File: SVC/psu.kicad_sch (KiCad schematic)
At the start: 32 parts, among them T1 760871543, U10 FODM217D, U11 TNY288D, U12 SI8932D-IS4, U13 AP7381-33SA-7

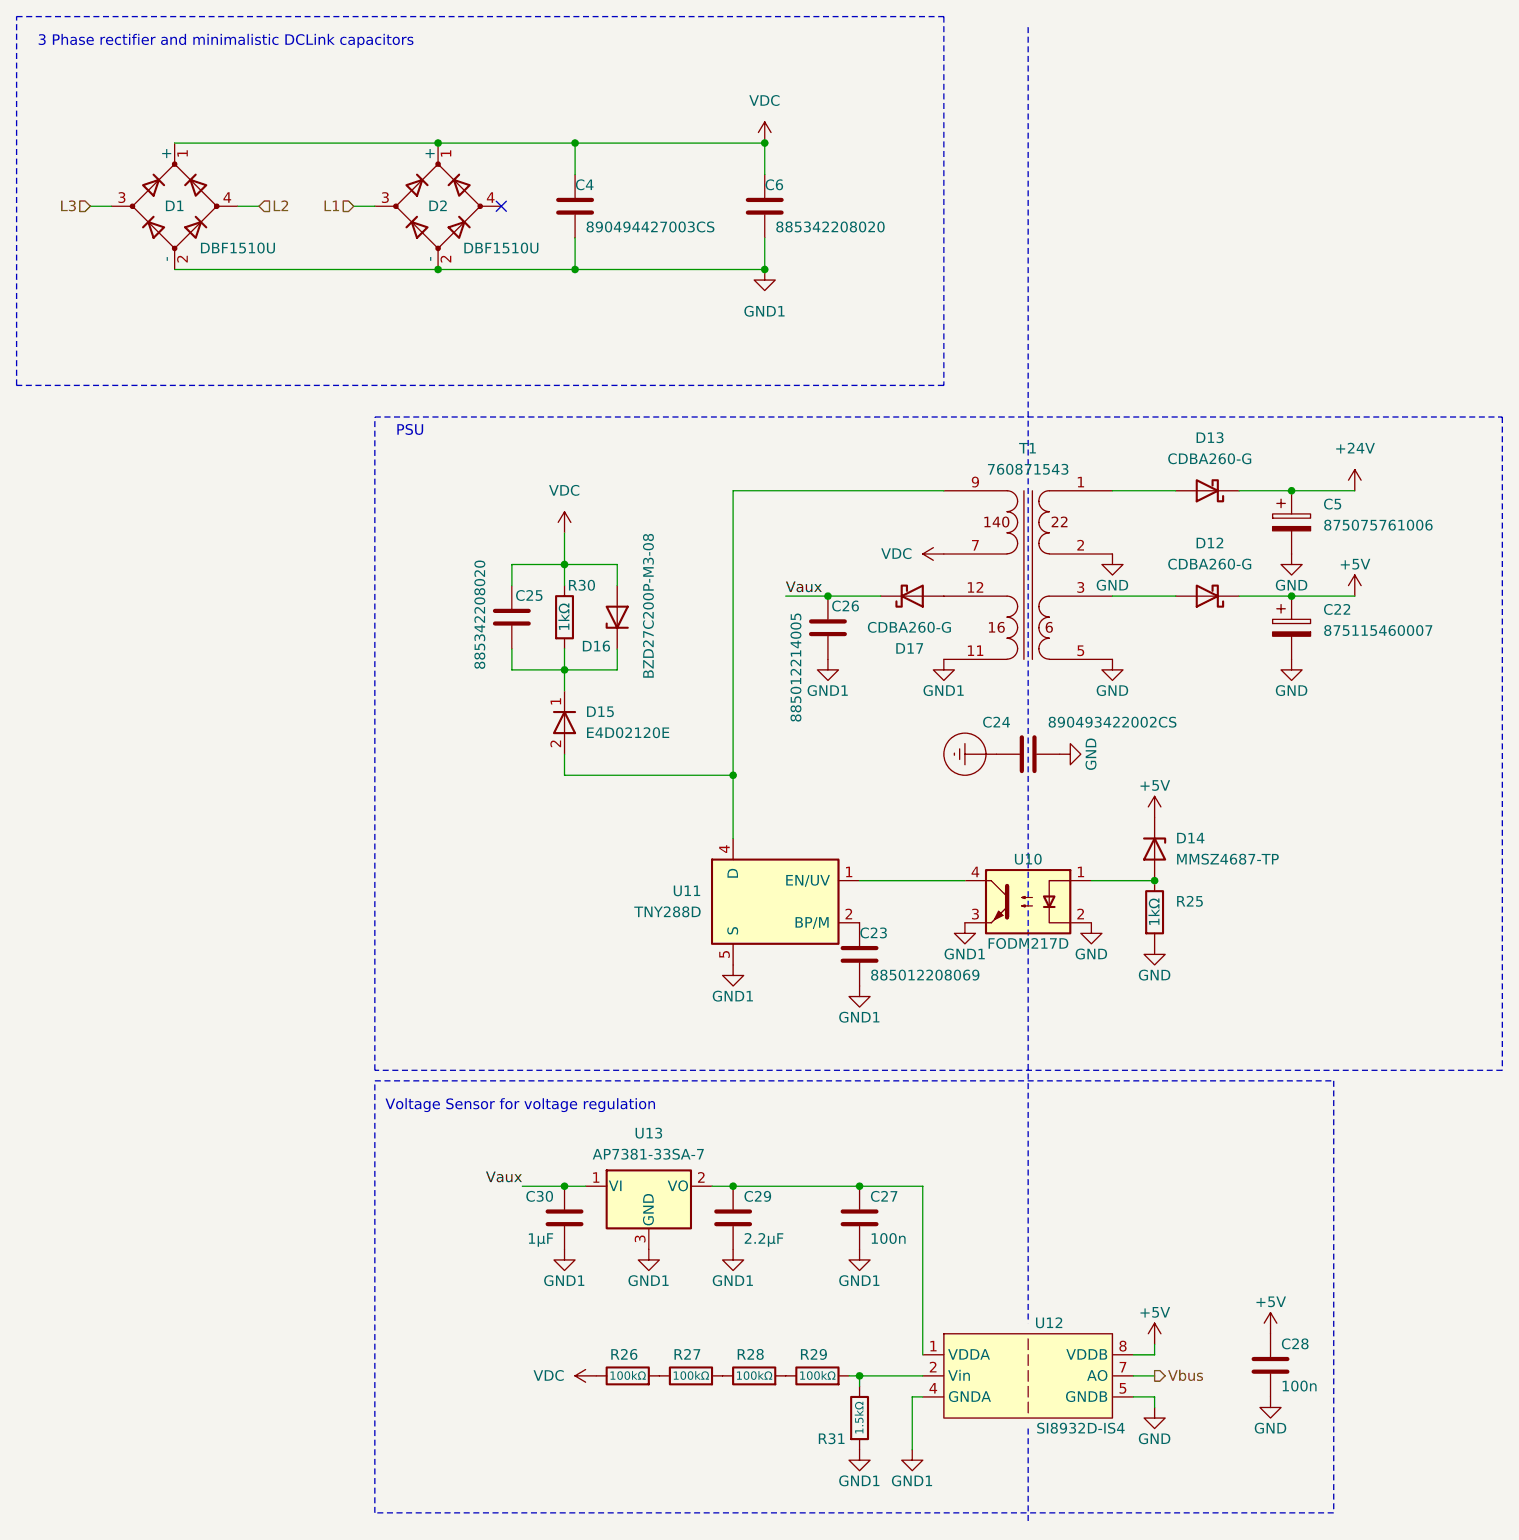
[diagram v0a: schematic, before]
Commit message: did some layout work, minor schematic changes to help with layout
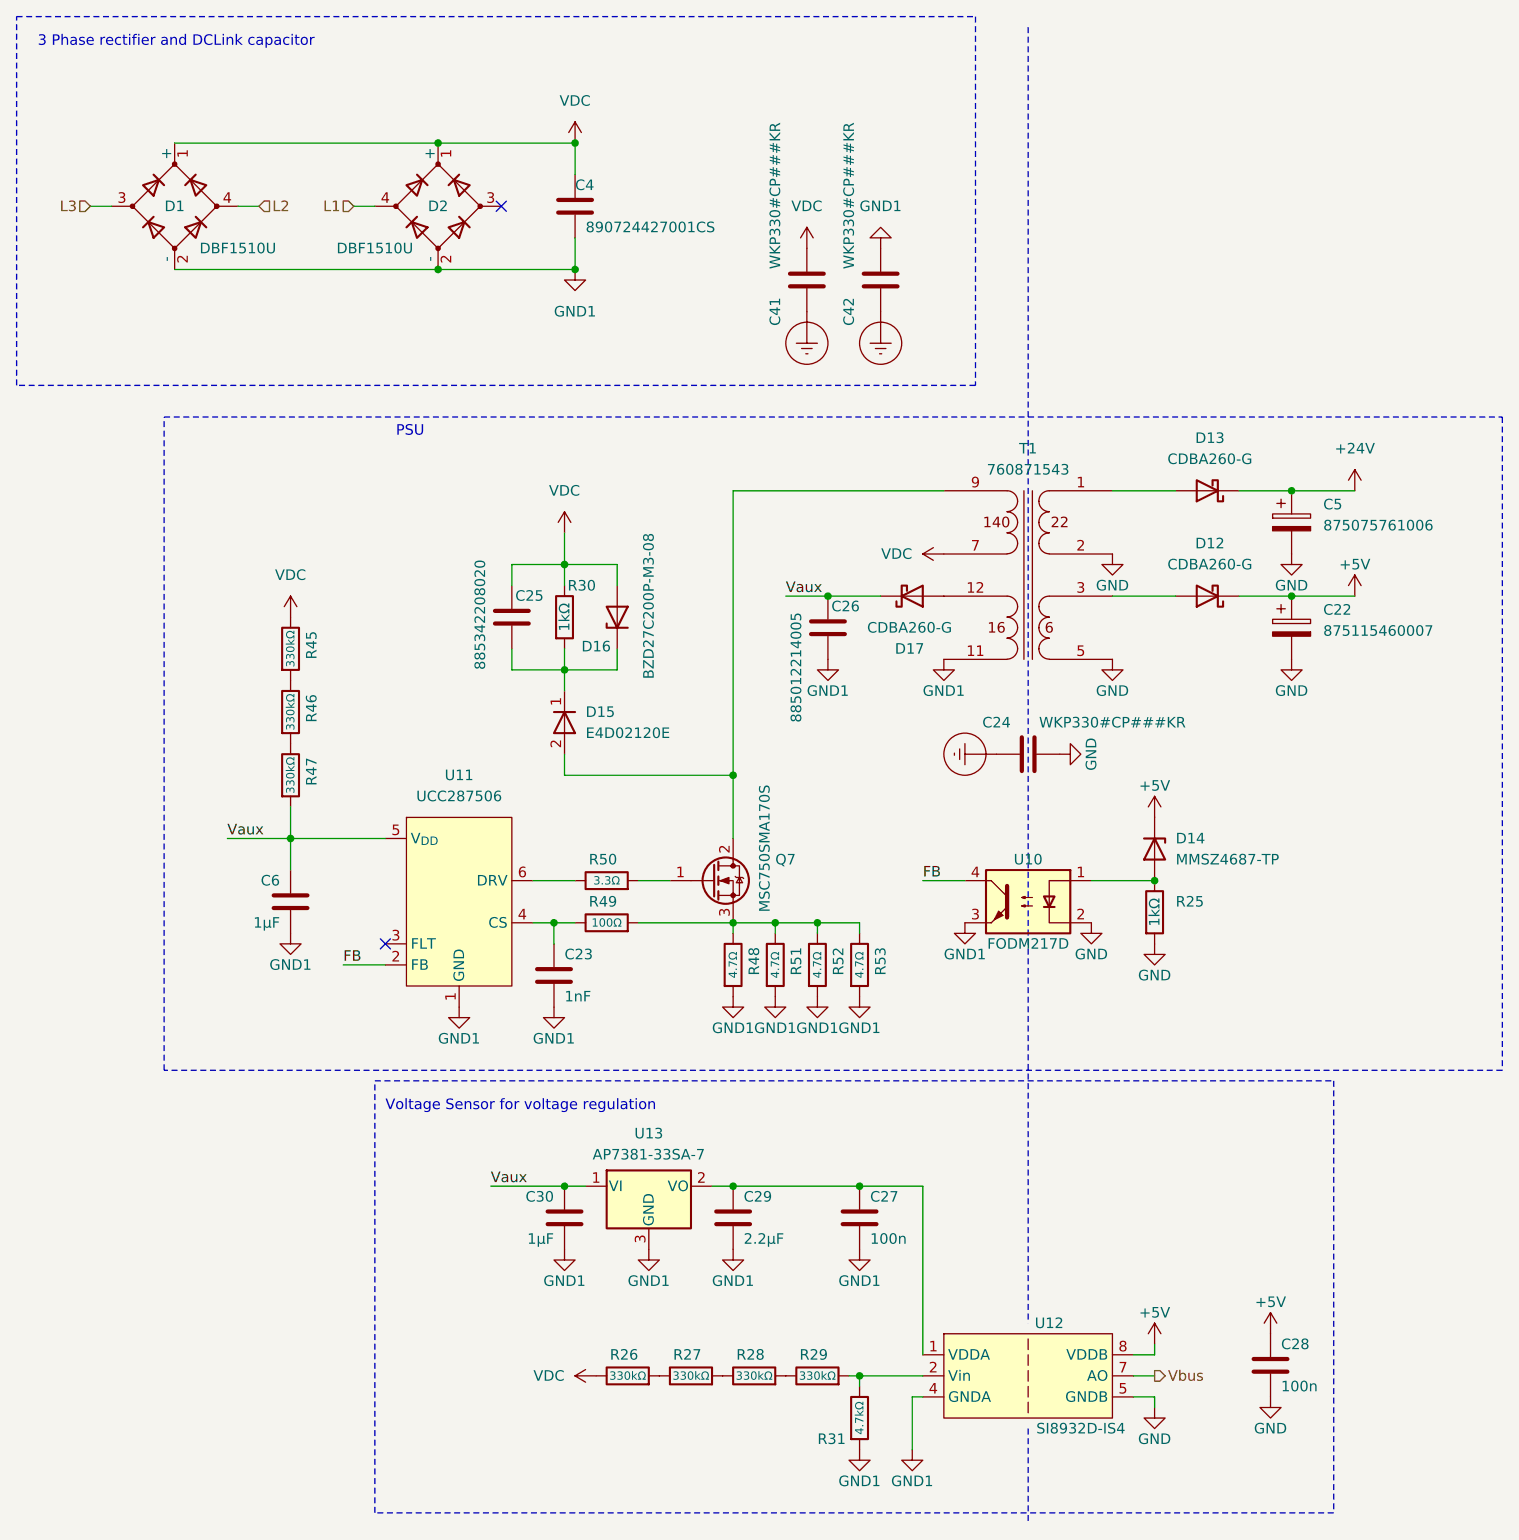
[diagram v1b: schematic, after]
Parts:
- removed U11: TNY288D, Package_SO:PowerIntegrations_SO-8C, symbol Regulator_Switching:TNY288D
- added C41, C42: WKP330#CP###KR, Footprints:WKP330#CP###KR, symbol Device:C
- added Q7: MSC750SMA170S, Package_TO_SOT_SMD:TO-252-2, symbol Device:Q_NMOS_GDS
- added R45, R46, R47: 330kΩ, Resistor_SMD:R_0805_2012Metric, symbol Device:R
- added R48, R51, R52, R53: 4.7Ω, Resistor_SMD:R_0805_2012Metric, symbol Device:R
- added R49: 100Ω, Resistor_SMD:R_0805_2012Metric, symbol Device:R
- added R50: 3.3Ω, Resistor_SMD:R_0805_2012Metric, symbol Device:R
- added U11: UCC287506, Package_TO_SOT_SMD:SOT-23-6, symbol parts:UCC28750X
- C23: value 885012208069 -> 1nF; footprint Capacitor_SMD:C_1206_3216Metric -> Capacitor_SMD:C_0805_2012Metric
- C24: value 890493422002CS -> WKP330#CP###KR; footprint Capacitor_THT:C_Rect_L10.3mm_W5.7mm_P7.50mm_MKS4 -> Footprints:WKP330#CP###KR
- C4: value 890494427003CS -> 890724427001CS; footprint Capacitor_THT:C_Rect_L33.0mm_W15.0mm_P27.50mm_MKS4 -> Capacitor_THT:C_Rect_L31.5mm_W9.0mm_P27.50mm_MKS4
- C6: value 885342208020 -> 1µF; footprint Capacitor_SMD:C_1206_3216Metric -> Capacitor_SMD:C_0805_2012Metric
- R26, R27, R28, R29: value 100kΩ -> 330kΩ
- R30: footprint Resistor_SMD:R_0805_2012Metric -> Resistor_SMD:R_1206_3216Metric
- R31: value 1.5kΩ -> 4.7kΩ
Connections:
- net Earth_Protective: now also C41.1, C42.1
- net GND1: now also C42.2, R48.2, R51.2, R52.2, R53.2, U11.1 (GND)
- net L1: now also D2.4; no longer D2.3
- net VDC: now also C41.2, R45.1; no longer C6.1
- net Vaux: now also C6.1, R47.2, U11.5 (V_{DD})
- net FB: now reaches U10.4
- net FB: now also U11.2 (FB)
- net at C23.1: now also R49.1, U11.4 (CS)
- net at D15.2 (A), T1.9 (IN+): now also Q7.2 (D)
- new net: Q7.3 (S), R48.1, R49.2, R51.1, R52.1, R53.1
- new net: R45.2, R46.1
- new net: R46.2, R47.1
- new net: R50.1, U11.6 (DRV)
- new net: Q7.1 (G), R50.2
- no-connect marks 1 -> 2
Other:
- note added: "3 Phase rectifier and DCLink capacitor"
- note removed: "3 Phase rectifier and minimalistic DCLink capacitors"
- moved on the sheet: D2
